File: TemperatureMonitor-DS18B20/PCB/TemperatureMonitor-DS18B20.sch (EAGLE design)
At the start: 16 parts, among them IC1 ESP8266MINI, IC2 MCP1700 3300, IC3 SSD1306, IC4 LM358, SW1 SensorID, SW2 DeepSleep, T1 DS18B20

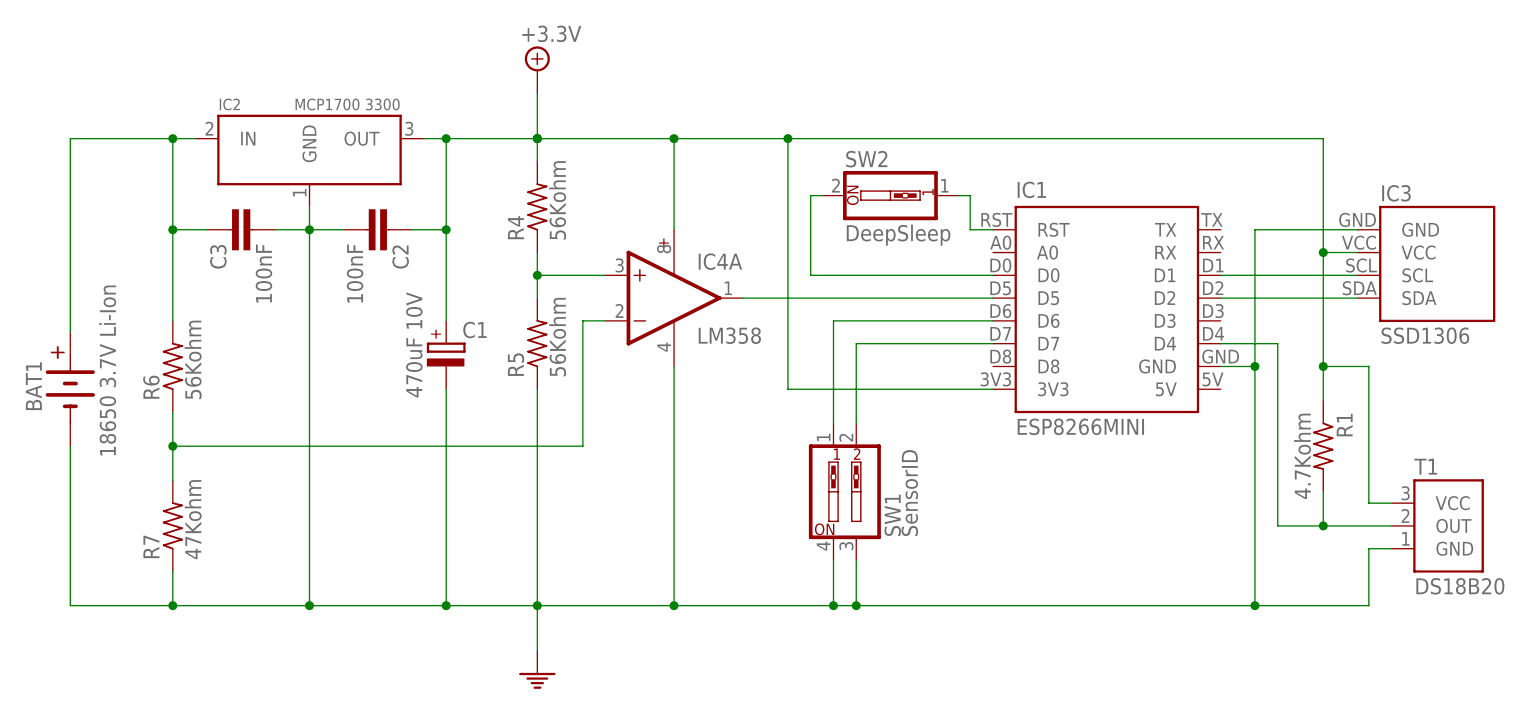
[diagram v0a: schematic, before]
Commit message: Battery status check via A/D on DS18B20 version
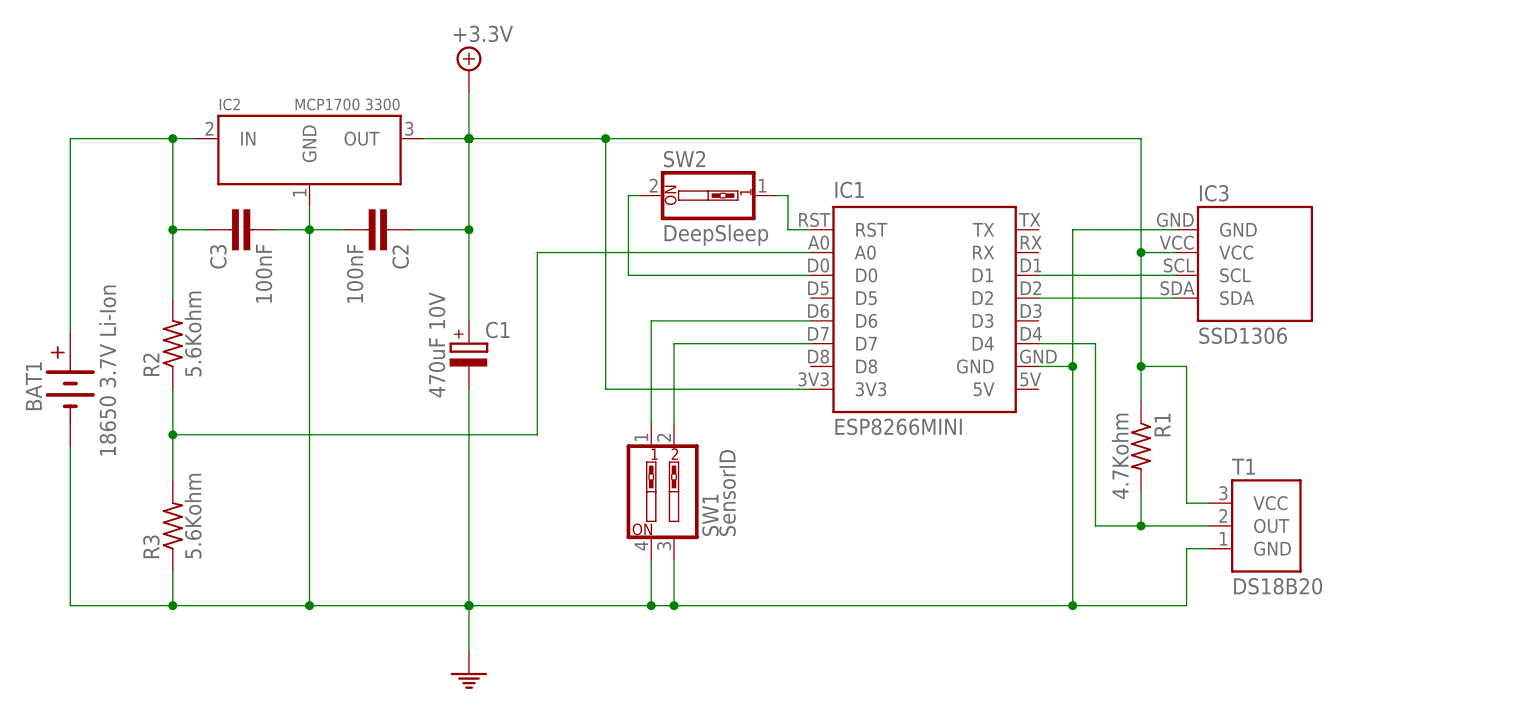
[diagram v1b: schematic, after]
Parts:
- removed IC4: LM358, wizzent:LM358
- removed R4, R5, R6: 56Kohm, wizzent:RESISTOR0.25W
- added R2: 5.6Kohm, wizzent:RESISTOR0.25W
- R3: value 47Kohm -> 5.6Kohm
- renumbered R7 to R3
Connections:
- removed net N$11: IC1.D5, IC4A.OUT
- removed net N$9: IC4A.+IN, R4.1, R5.2
- net +3.3V: no longer IC4G$3.V+, R4.2
- net GND: no longer IC4G$3.V-, R5.1
- net N$10: now also IC1.A0, R2.1; no longer IC4A.-IN, R6.1
- net N$3: now also R2.2; no longer R6.2
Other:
- moved on the sheet: C1, IC1, IC3, R1, SW1, SW2, T1

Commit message: Minor changes
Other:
- moved on the sheet: C1, IC3, R1, SW1, T1
